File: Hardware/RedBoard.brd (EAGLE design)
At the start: 68.6 x 54.4 mm, 65 parts, among them IC3 LM1117, J1 POWER_JACKOVERPASTE_REDBOARD_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, J2 ICSP, Q1 ZXMP6A13FTA, Q2 2N7002PW, U1 FT231XS, U2 MIC5205, U3 ATMEGA328, Y1 16MHz

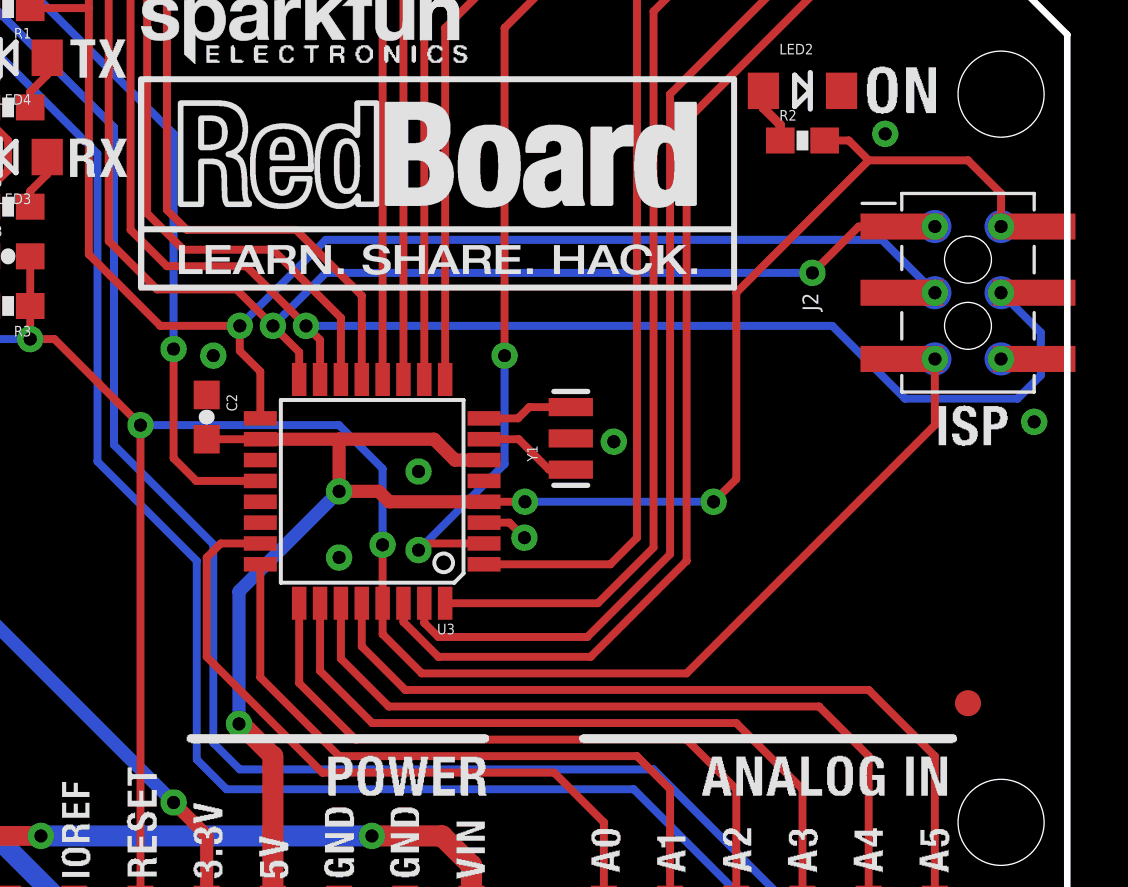
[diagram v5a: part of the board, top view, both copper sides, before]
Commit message: Moving vias off programming test points
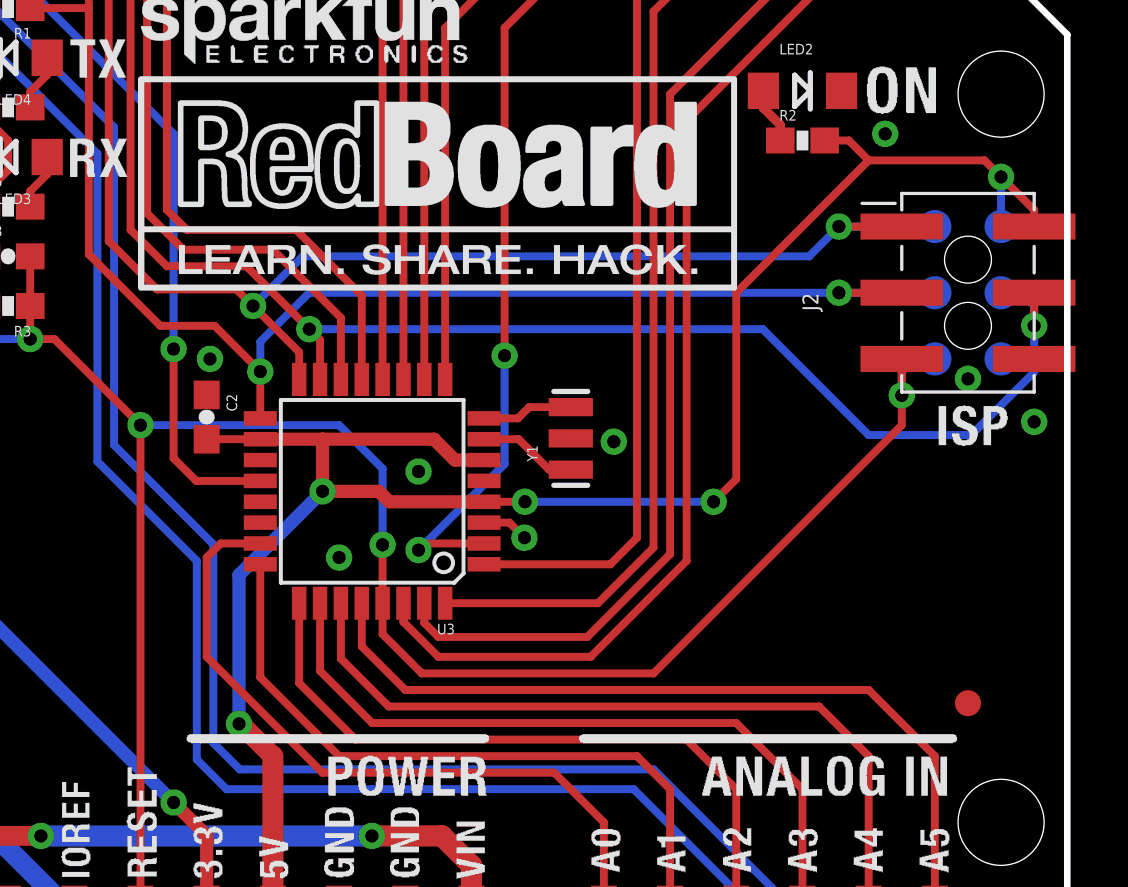
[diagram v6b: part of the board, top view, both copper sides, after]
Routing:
- net MISO: track 59.8 -> 62.6 mm, vias 3 -> 2
- net 5V: track 165.7 -> 167.6 mm
- net MOSI: track 68.0 -> 69.0 mm
